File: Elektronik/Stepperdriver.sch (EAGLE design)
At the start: 28 parts, among them IC1 MEGA8-AI

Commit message: Elektronik auf den neusten Stand gebracht (Merge mit privater Dropbox
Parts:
- removed ADDR_A, ADDR_B, STPCLK_A, STPCLK_B: 219-10, switch-dil:219-10
- removed IC1: MEGA8-AI, atmel:MEGA8-AI
- added ADDA, ADDB, SCLKA, SCLKB: 219-08, switch-dil:219-08
- added C10, C5: 100µ, rcl:CPOL-EU150CLZ-1010
- added C11, C6: 220n, rcl:C-EUC0805
- added C12, C7, C8, C9: 100n, rcl:C-EUC0805
- added C_REGA, C_REGB: 22µ, rcl:C-EUC0805
- added R4, R5: 1k, rcl:R-EU_R0805
- added R6, R7: 1M, rcl:R-EU_R0805
- C2, C4: value 10n -> 220n
- H1, H2, H3, H4: value MOUNT-HOLE5.0 -> MOUNT-PAD-ROUND5.0; device holes:MOUNT-HOLE5.0 -> holes:MOUNT-PAD-ROUND5.0
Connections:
- net N$101 renamed IO113
- net N$102 renamed IO111
- net N$103 renamed IO109
- net N$104 renamed IO107
- net N$105 renamed IO105
- net N$106 renamed IO103
- net N$107 renamed IO101
- net N$108 renamed IO99
- net N$109 renamed IO97
- net N$110 renamed IO95
- net N$111 renamed IO93
- net N$112 renamed IO91
- net N$113 renamed IO89
- net N$114 renamed IO87
- net N$115 renamed IO85
- net N$116 renamed IO83
- net N$117 renamed IO81
- net N$118 renamed IO79
- net N$119 renamed IO77
- net N$12 renamed IO16
- net N$120 renamed IO75
- net N$121 renamed IO54
- net N$122 renamed IO56
- net N$123 renamed IO58
- net N$124 renamed IO60
- net N$125 renamed IO62
- net N$126 renamed IO64
- net N$127 renamed IO66
- net N$128 renamed IO68
- net N$129 renamed IO70
- net N$13 renamed IO18
- net N$130 renamed IO72
- net N$131 renamed IO55
- net N$132 renamed IO57
- net N$133 renamed IO59
- net N$134 renamed IO61
- net N$135 renamed IO63
- net N$136 renamed IO65
- net N$137 renamed IO67
- net N$138 renamed IO69
- net N$139 renamed IO71
- net N$14 renamed IO20
- net N$140 renamed IO73
- net N$141 renamed IO35
- net N$142 renamed IO37
- net N$143 renamed IO39
- net N$144 renamed IO41
- net N$145 renamed IO43
- net N$146 renamed IO45
- net N$147 renamed IO47
- net N$148 renamed IO49
- net N$149 renamed IO51
- net N$15 renamed IO22
- net N$150 renamed IO53
- net N$151 renamed IO34
- net N$152 renamed IO36
- net N$153 renamed IO38
- net N$154 renamed IO40
- net N$155 renamed IO42
- net N$156 renamed IO44
- net N$157 renamed IO46
- net N$158 renamed IO48
- net N$159 renamed IO50
- net N$16 renamed IO24
- net N$160 renamed IO52
- net N$17 renamed IO26
- net N$18 renamed IO28
- net N$19 renamed IO30
- net N$20 renamed IO32
- net N$32 renamed IO17
- net N$33 renamed IO19
- net N$34 renamed IO21
- net N$35 renamed IO23
- net N$36 renamed IO25
- net N$37 renamed IO27
- net N$38 renamed IO29
- net N$39 renamed IO31
- net N$40 renamed IO33
- net N$41 renamed IO74
- net N$42 renamed IO76
- net N$43 renamed IO78
- net N$44 renamed IO80
- net N$45 renamed IO82
- net N$46 renamed IO84
- net N$47 renamed IO86
- net N$48 renamed IO88
- net N$49 renamed IO90
- net N$50 renamed IO92
- net N$51 renamed IO94
- net N$52 renamed IO96
- net N$53 renamed IO98
- net N$54 renamed IO100
- net N$55 renamed IO102
- net N$56 renamed IO104
- net N$57 renamed IO106
- net N$58 renamed IO108
- net N$59 renamed IO110
- net N$60 renamed IO112
- removed net N$10: SV2.20
- removed net N$100: IC1.PD0(RXD)
- removed net N$11: SV2.22
- removed net N$161: IC1.PD1(TXD)
- removed net N$162: IC1.PD2(INT0)
- removed net N$163: IC1.PD3(INT1)
- removed net N$164: IC1.PD4(XCK/T0)
- removed net N$165: IC1.PD5(T1)
- removed net N$166: IC1.PD6(AIN0)
- removed net N$167: IC1.PD7(AIN1)
- removed net N$21: SV2.1
- removed net N$22: SV2.3
- removed net N$23: SV2.5
- removed net N$24: SV2.7
- removed net N$25: SV2.9
- removed net N$26: SV2.11
- removed net N$27: SV2.13
- removed net N$28: SV2.15
- removed net N$29: SV2.17
- removed net N$30: SV2.19
- removed net N$31: SV2.21
- removed net N$64: U$2.OUT2B, X1-8.KL
- removed net N$65: U$2.OUT1B, X1-9.KL
- removed net N$69: U$1.OUT1A, X1-3.KL
- removed net N$7 (its old number): SV2.14
- removed net N$70: U$1.OUT2A, X1-4.KL
- removed net N$72: U$1.OUT1B, X1-5.KL
- removed net N$73: U$1.OUT2B, X1-6.KL
- removed net N$79: A_BUSY.C
- removed net N$8 (its old number): SV2.16
- removed net N$80: B_BUSY.C
- removed net N$81: FAULT.C
- removed net N$85: ADDR_A.1, ADDR_B.1, STPCLK_A.1, STPCLK_B.1
- removed net N$86: ADDR_A.2, ADDR_B.2, STPCLK_A.2, STPCLK_B.2
- removed net N$87: ADDR_A.3, ADDR_B.3, STPCLK_A.3, STPCLK_B.3
- removed net N$88: ADDR_A.4, ADDR_B.4, STPCLK_A.4, STPCLK_B.4
- removed net N$89: ADDR_A.5, ADDR_B.5, STPCLK_A.5, STPCLK_B.5
- removed net N$9: SV2.18
- removed net N$90: ADDR_A.6, ADDR_B.6, STPCLK_A.6, STPCLK_B.6
- removed net N$91: ADDR_A.7, ADDR_B.7, STPCLK_A.7, STPCLK_B.7
- removed net N$92: ADDR_A.8, ADDR_B.8, STPCLK_A.8, STPCLK_B.8
- removed net N$93: ADDR_A.9, ADDR_B.9, STPCLK_A.9, STPCLK_B.9
- removed net N$94: ADDR_A.10, ADDR_B.10, STPCLK_A.10, STPCLK_B.10
- removed net N$95: IC1.PC3(ADC3)
- removed net N$96: IC1.PC4(ADC4/SDA)
- removed net N$97: IC1.PC5(ADC5/SCL)
- removed net N$98: IC1.ADC6
- removed net N$99: IC1.ADC7
- removed net SW_A: U$1.SW, X1-7.KL
- new net IO0: ADDA.1, ADDB.1, SV2.8
- new net IO1: ADDA.2, ADDB.2, SV2.7
- new net IO10: SCLKA.3, SCLKB.3, SV2.18
- new net IO11: SCLKA.4, SCLKB.4, SV2.17
- new net IO12: SCLKA.5, SCLKB.5, SV2.20
- new net IO13: SCLKA.6, SCLKB.6, SV2.19
- new net IO14: SCLKA.7, SCLKB.7, SV2.22
- new net IO15: SCLKA.8, SCLKB.8, SV2.21
- new net IO2: ADDA.3, ADDB.3, SV2.10
- new net IO3: ADDA.4, ADDB.4, SV2.9
- new net IO4: ADDA.5, ADDB.5, SV2.12
- new net IO5: ADDA.6, ADDB.6, SV2.11
- new net IO6: ADDA.7, ADDB.7, SV2.14
- new net IO7: ADDA.8, ADDB.8, SV2.13
- new net IO8: SCLKA.1, SCLKB.1, SV2.16
- new net IO9: SCLKA.2, SCLKB.2, SV2.15
- net !CS_A: now also ADDA.10, ADDA.11, ADDA.12, ADDA.13, ADDA.14, ADDA.15, ADDA.16, ADDA.9; no longer ADDR_A.11, ADDR_A.12, ADDR_A.13, ADDR_A.14, ADDR_A.15, ADDR_A.16, ADDR_A.17, ADDR_A.18, ADDR_A.19, ADDR_A.20
- net !CS_B: now also ADDB.10, ADDB.11, ADDB.12, ADDB.13, ADDB.14, ADDB.15, ADDB.16, ADDB.9; no longer ADDR_B.11, ADDR_B.12, ADDR_B.13, ADDR_B.14, ADDR_B.15, ADDR_B.16, ADDR_B.17, ADDR_B.18, ADDR_B.19, ADDR_B.20
- net !FLAG: now also FAULT.C
- net +3V3: now also C12.1, C7.1, C_REGA.1, C_REGB.1, SV2.2, SV2.4, SV2.6
- net BUSY_A: now also A_BUSY.C
- net BUSY_B: now also B_BUSY.C
- net GND: now also C10.-, C11.2, C12.2, C5.-, C6.2, C7.2, C8.2, C9.2, C_REGA.2, C_REGB.2, H1.MOUNT, H2.MOUNT, H3.MOUNT, H4.MOUNT, R6.2, R7.2, SV2.1, SV2.3, SV2.5
- net N$1: now also U$1.OUT1A, X1-6.KL; no longer SV2.2
- net N$2: now also U$1.OUT2A, X1-5.KL; no longer SV2.4
- net N$3: now also U$1.OUT1B, X1-3.KL; no longer SV2.6
- net N$4: now also U$1.OUT2B, X1-4.KL; no longer SV2.8
- net N$5: now also U$2.OUT2B, X1-9.KL; no longer SV2.10
- net N$6: now also U$2.OUT1B, X1-8.KL; no longer SV2.12
- net N$76: now also R5.1; no longer U$2.SW
- net N$82: now also C9.1, R5.2, R7.1, U$2.SW; no longer IC1.PC0(ADC0)
- net N$83: now also C8.1, R4.2, R6.1, U$1.SW; no longer IC1.PC1(ADC1)
- net N$84: now also R4.1, X1-7.KL; no longer IC1.PC2(ADC2)
- net STEPCLOCK_A: now also SCLKA.10, SCLKA.11, SCLKA.12, SCLKA.13, SCLKA.14, SCLKA.15, SCLKA.16, SCLKA.9; no longer STPCLK_A.11, STPCLK_A.12, STPCLK_A.13, STPCLK_A.14, STPCLK_A.15, STPCLK_A.16, STPCLK_A.17, STPCLK_A.18, STPCLK_A.19, STPCLK_A.20
- net STEPCLOCK_B: now also SCLKB.10, SCLKB.11, SCLKB.12, SCLKB.13, SCLKB.14, SCLKB.15, SCLKB.16, SCLKB.9; no longer STPCLK_B.11, STPCLK_B.12, STPCLK_B.13, STPCLK_B.14, STPCLK_B.15, STPCLK_B.16, STPCLK_B.17, STPCLK_B.18, STPCLK_B.19, STPCLK_B.20
- net V+: now also C10.+, C11.1, C5.+, C6.1
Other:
- moved on the sheet: A_BUSY, B_BUSY, FAULT, H1, H2, H3, H4, R1, R2, R3, SV1, SV2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

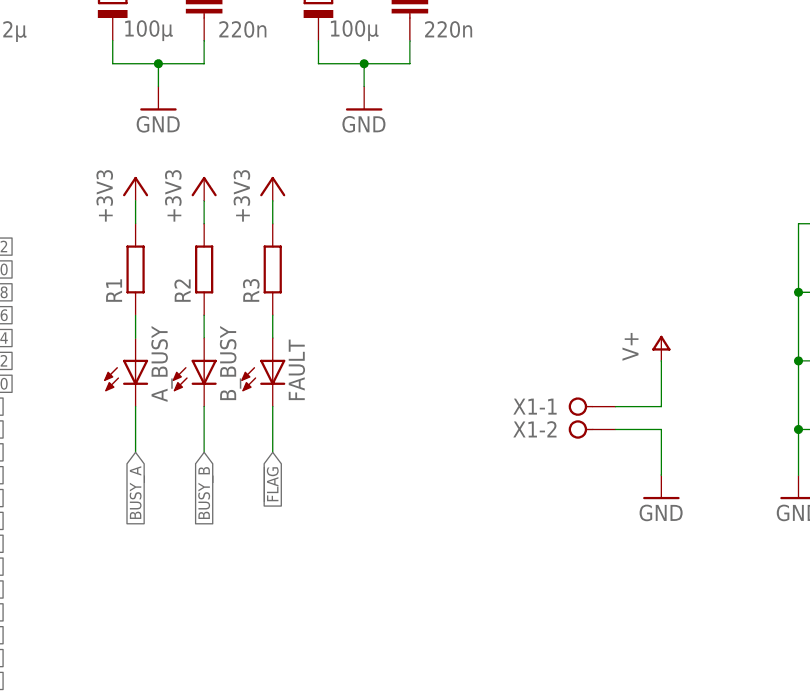
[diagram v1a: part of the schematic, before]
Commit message: Stepperendstufe weitergeroutet
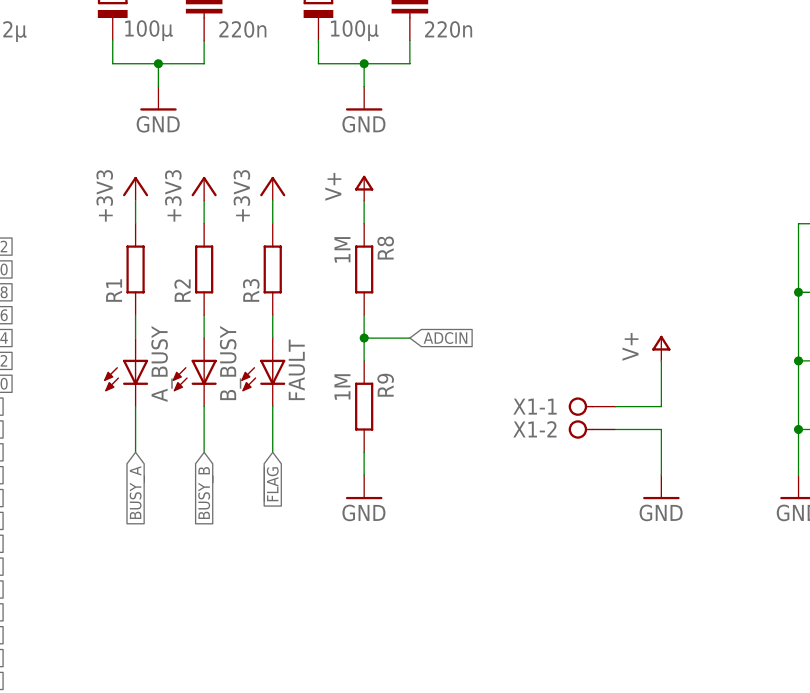
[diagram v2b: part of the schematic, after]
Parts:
- added R8, R9: 1M, rcl:R-EU_R0805
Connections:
- net ADCIN: now also R8.2, R9.1
- net GND: now also R9.2
- net V+: now also R8.1
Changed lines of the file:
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@@
 <part name="ADDB" library="switch-dil" deviceset="219-08*" device=""/>
 <part name="ADDA" library="switch-dil" deviceset="219-08*" device=""/>
+<part name="R8" library="rcl" deviceset="R-EU_" device="R0805" value="1M"/>
+<part name="R9" library="rcl" deviceset="R-EU_" device="R0805" value="1M"/>
+<part name="P+6" library="supply1" deviceset="V+" device=""/>
+<part name="GND16" library="supply1" deviceset="GND" device=""/>
 </parts>
 <sheets>
@@
 <instance part="ADDB" gate="G$1" x="27.94" y="119.38" rot="R270"/>
 <instance part="ADDA" gate="G$1" x="27.94" y="149.86" rot="R270"/>
+<instance part="R8" gate="G$1" x="190.5" y="55.88" rot="R270"/>
+<instance part="R9" gate="G$1" x="190.5" y="40.64" rot="R270"/>
+<instance part="P+6" gate="1" x="190.5" y="66.04"/>
+<instance part="GND16" gate="1" x="190.5" y="30.48"/>
 </instances>
 <busses>
@@
 <wire x1="71.12" y1="48.26" x2="66.04" y2="48.26" width="0.1524" layer="91"/>
 <wire x1="66.04" y1="48.26" x2="66.04" y2="43.18" width="0.1524" layer="91"/>
+</segment>
+<segment>
+<pinref part="R9" gate="G$1" pin="2"/>
+<pinref part="GND16" gate="1" pin="GND"/>
+<wire x1="190.5" y1="35.56" x2="190.5" y2="33.02" width="0.1524" layer="91"/>
 </segment>
 </net>
@@
 <junction x="190.5" y="91.44"/>
 </segment>
+<segment>
+<pinref part="P+6" gate="1" pin="V+"/>
+<pinref part="R8" gate="G$1" pin="1"/>
+<wire x1="190.5" y1="63.5" x2="190.5" y2="60.96" width="0.1524" layer="91"/>
+</segment>
 </net>
 <net name="ADCIN" class="0">
@@
 <label x="220.98" y="121.92" size="1.27" layer="95" xref="yes"/>
 </segment>
-</net>
+<segment>
+<pinref part="R8" gate="G$1" pin="2"/>
+<pinref part="R9" gate="G$1" pin="1"/>
+<wire x1="190.5" y1="50.8" x2="190.5" y2="48.26" width="0.1524" layer="91"/>
+<wire x1="190.5" y1="48.26" x2="190.5" y2="45.72" width="0.1524" layer="91"/>
+<wire x1="190.5" y1="48.26" x2="195.58" y2="48.26" width="0.1524" layer="91"/>
+<junction x="190.5" y="48.26"/>
+<label x="195.58" y="48.26" size="1.27" layer="95" xref="yes"/>
+</segment>
+</net>
